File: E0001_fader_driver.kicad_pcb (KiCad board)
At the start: 4 copper layers, 107 x 17 mm, 34 parts, among them J1 JST GH SM04B-GHS-TB, J2 TC2030-IDC-NL, Q1 AO3401A, U1 STM32C051F6P6, U2 MCP1703A-3302E/CB, U3 DRV8210PDSGR

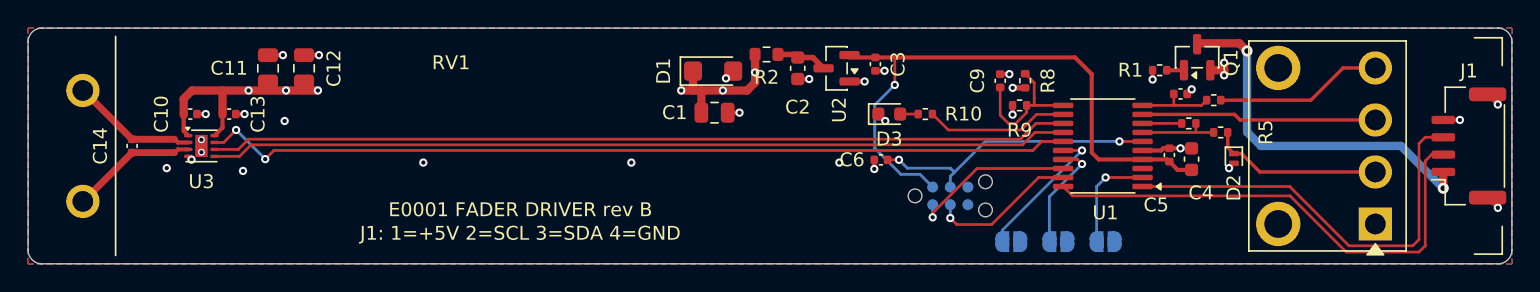
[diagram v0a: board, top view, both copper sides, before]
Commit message: E0001 rev C: PBUS v2 input, local eFuse, UART bootloader header, fab outputs
- Supply from E0003 peripheral bus v2 (PBUS 6-9 V) instead of 5 V
- TPS259470A local eFuse (OVLO, 0.6 A limit, reverse blocking); SMF9.0A after eFuse
- MCP1703A SOT-89 LDO; DRV8210 logic on 3V3
- Tag-Connect SWD replaced by 1x6 right-angle UART bootloader header (J2)
- No test points; common cross-project parts; PBUS 6-9 V silkscreen
- Rev B archived in archive/revB; fab outputs in fab/E0001_revB and fab/E0001_revC
- Spec docs/SPEC_revC.md v1.0, schematic notes, layout review r1 (PASS)

Co-Authored-By: Claude Opus 5.5 <noreply@anthropic.com>
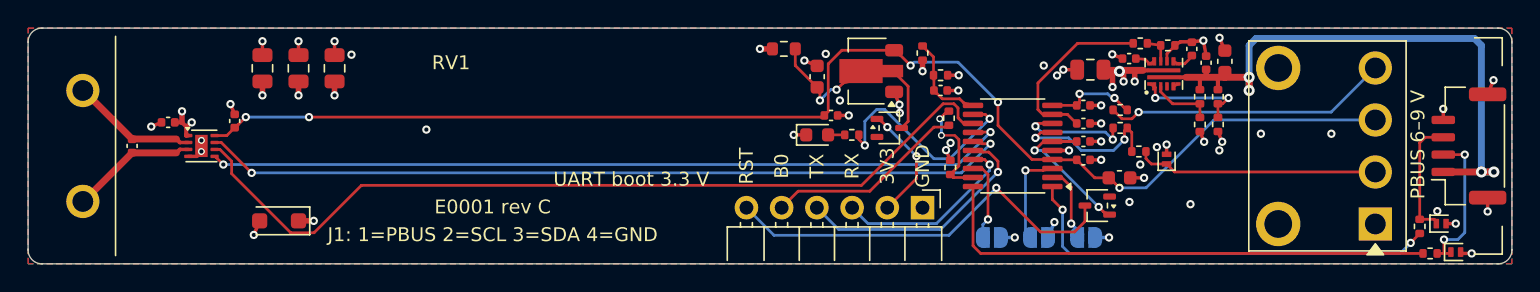
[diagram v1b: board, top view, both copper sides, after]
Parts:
- removed Q1: AO3401A, Package_TO_SOT_SMD:SOT-23
- removed R1: 10k, Resistor_SMD:R_0402_1005Metric
- added C15: 4.7nF, Capacitor_SMD:C_0402_1005Metric, F.Cu at (145.9, 93.7)
- added C16: 1.8nF, Capacitor_SMD:C_0402_1005Metric, F.Cu at (150.4, 93.0)
- added C17: 100nF, Capacitor_SMD:C_0402_1005Metric, F.Cu at (151.4, 94.0)
- added C18: 4.7uF, Capacitor_SMD:C_0603_1608Metric, F.Cu at (152.8, 93.9)
- added C19: 1nF, Capacitor_SMD:C_0402_1005Metric, F.Cu at (142.6, 98.4)
- added C20: 10uF, Capacitor_SMD:C_0805_2012Metric, F.Cu at (88.6, 94.4)
- added D4: PESD5V0L1UL, Diode_SMD:D_SOD-882, F.Cu at (169.4, 107.7)
- added D5: PESD5V0L1UL, Diode_SMD:D_SOD-882, F.Cu at (168.4, 105.6)
- added D6: BAT54W, Package_TO_SOT_SMD:SOT-323_SC-70, F.Cu at (143.6, 104.3)
- added D7: BAT54W, Package_TO_SOT_SMD:SOT-323_SC-70, F.Cu at (128.6, 98.7)
- added R11: 1M 1%, Resistor_SMD:R_0402_1005Metric, F.Cu at (152.3, 96.5)
- added R12: 330k 1%, Resistor_SMD:R_0402_1005Metric, F.Cu at (152.3, 98.5)
- added R13: 1M 1%, Resistor_SMD:R_0402_1005Metric, F.Cu at (151.0, 96.5)
- added R14: 137k 1%, Resistor_SMD:R_0402_1005Metric, F.Cu at (151.0, 98.5)
- added R15: 5.23k 1%, Resistor_SMD:R_0402_1005Metric, F.Cu at (148.7, 92.8)
- added R16: 10k, Resistor_SMD:R_0402_1005Metric, F.Cu at (146.7, 92.6)
- added R17: 10k, Resistor_SMD:R_0402_1005Metric, F.Cu at (133.0, 101.5)
- added R18: 1k, Resistor_SMD:R_0402_1005Metric, F.Cu at (132.9, 98.0)
- added R19: 0R, Resistor_SMD:R_0402_1005Metric, F.Cu at (167.6, 107.8)
- added R20: 0R, Resistor_SMD:R_0402_1005Metric, F.Cu at (166.8, 105.8)
- added U4: TPS259470ARPW, E0001:TI_RPW0010A_VQFN-HR-10_2x2mm_P0.475mm, F.Cu at (148.4, 94.8)
- C11, C12: value 22uF -> 10uF
- D1: value SMF5V0A -> SMF9.0A; footprint Diode_SMD:D_SMF -> Diode_SMD:D_SOD-123F
- J1: value JST GH SM04B-GHS-TB -> SM04B-GHS-TB
- J2: value TC2030-IDC-NL -> 61300611021; footprint Connector:Tag-Connect_TC2030-IDC-NL_2x03_P1.27mm_Vertical -> Connector_PinHeader_2.54mm:PinHeader_1x06_P2.54mm_Horizontal; moved to F.Cu
- R9: value 100k -> 30.1k 1%
- U2: value MCP1703A-3302E/CB -> MCP1703AT-3302E/MB; footprint Package_TO_SOT_SMD:SOT-23 -> Package_TO_SOT_SMD:SOT-89-3
- moved D1 33.1 mm to (84.6, 105.4), turned to 180 degrees
- moved C1 27.3 mm to (143.1, 94.5), turned to 180 degrees
- moved C6 14.7 mm to (142.6, 99.7), turned to 0 degrees
- moved R8 7.67 mm to (131.0, 93.3)
- moved C7 7.05 mm to (142.6, 97.1)
- moved R7 6.79 mm to (145.2, 97.4), turned to 0 degrees
- moved U1 6.50 mm to (137.5, 100.0)
- moved C4 6.21 mm to (142.6, 101.0), turned to 0 degrees
- moved R9 6.10 mm to (132.3, 94.9), turned to 0 degrees
- moved R5 6.06 mm to (146.6, 100.4)
- moved R10 5.51 mm to (125.9, 99.2)
- moved D3 5.41 mm to (123.4, 99.2)
- moved C5 5.37 mm to (145.2, 102.3), turned to 0 degrees
- moved R6 4.96 mm to (145.2, 98.7)
- moved C3 4.89 mm to (124.4, 97.8), turned to 0 degrees
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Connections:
- C1 pad 1: +5V -> VM_P
- C10 pad 1: +5V -> +3V3
- C11 pad 1: +5V -> VM_P
- C12 pad 1: +5V -> VM_P
- C13 pad 1: +5V -> VM_P
- D1 pad 1: +5V -> VM_P
- J1 pad 1: /VIN -> /PBUS_IN
- J1 pad 2: /I2C_SCL -> /J1_SCL
- J1 pad 3: /I2C_SDA -> /J1_SDA
- J2 pad 1: +3V3 -> GND
- J2 pad 2: /SWDIO -> /J2_3V3
- J2 pad 3: /NRST -> /UART_RX
- J2 pad 4: /SWCLK -> /UART_TX
- J2 pad 5: GND -> /J2_BOOT0
- J2 pad 6: unconnected-(J2-SWO-Pad6) -> /J2_NRST
- R2 pad 1: +5V -> VM_P
- R8 pad 1: +5V -> VM_P
- RV1 pad 3: /POT_HI -> +3V3
- U1 pad 16: /ADDR0 -> /UART_TX
- U1 pad 17: /ADDR1 -> /UART_RX
- U1 pad 18: /SWDIO -> /ADDR0
- U1 pad 19: /SWCLK -> /BOOT0
- U1 pad 3: unconnected-(U1-PC15-Pad3) -> /ADDR1
- U1 pad 9: /POT_HI -> /ILM_ADC
- U2 pad 2: +3V3 -> /LDO_IN
- U2 pad 3: /LDO_IN -> +3V3
- U3 pad 1: +5V -> VM_P
- U3 pad 8: +5V -> +3V3
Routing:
- net +3V3: track 43.8 -> 95.5 mm, vias 1 -> 5
- net /PBUS_IN: track 0.00 -> 42.7 mm, vias 0 -> 4
- net +5V: track 29.6 -> 0.00 mm, vias 9 -> 0
- net /J2_NRST: track 0.00 -> 29.4 mm, vias 0 -> 1
- net /VIN: track 26.7 -> 0.00 mm, vias 2 -> 0
- net /UART_TX: track 0.00 -> 18.3 mm, vias 0 -> 1
- net /POT_HI: track 17.0 -> 0.00 mm
- net GND: track 19.1 -> 34.9 mm, vias 29 -> 52
- net VM_P: track 0.00 -> 14.8 mm, vias 0 -> 12
- net /J2_BOOT0: track 0.00 -> 14.5 mm
- net /UART_RX: track 0.00 -> 13.8 mm, vias 0 -> 1
- net /ILM_ADC: track 0.00 -> 12.5 mm
- net /SWDIO: track 12.0 -> 0.00 mm, vias 1 -> 0
- net /LDO_IN: track 3.70 -> 15.1 mm, vias 0 -> 2
- net /J1_SCL: track 0.00 -> 10.9 mm, vias 0 -> 2
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- added copper zone on In2.Cu, net VM_P
- removed copper zone on In2.Cu, net +5V
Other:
- board text added: "3V3"
- board text added: "A0"
- board text added: "A1"
- board text added: "A2"
- board text added: "B0"
- board text added: "E0001 rev C"
- board text added: "GND"
- board text added: "J1: 1=PBUS 2=SCL 3=SDA 4=GND"
- board text added: "PBUS 6–9 V"
- board text added: "RST"
- board text added: "RX"
- board text added: "TX"
- board text added: "UART boot 3.3 V"
- board text added: "addr 0x30–0x37, open = 1"
- board text removed: "ADDR: bridge=0"
- board text removed: "E0001 FADER DRIVER rev B"
- board text removed: "J1: 1=+5V 2=SCL 3=SDA 4=GND"
- board text removed: "SWD (TC2030)"

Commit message: Rev C hand-route experiment: strip, scripted pre-route, Freerouting, cleanup
All tracks and vias of the rev C board removed; placement, footprints,
zones and net classes unchanged. Own scripts (build/hr, preroute_c.py)
hand-route the motor loop, U3 supply, eFuse U4 PBUS_IN/VM_P power,
the PBUS feed from J1, the touch nets, and a plane via for every
GND/VM_P SMD pad. Freerouting 2.5.0 routes the rest; cleanup.py rebuilds
the chains as 45-degree paths. Not TraceMaker. Some joins still to fix.

Co-Authored-By: Claude Opus 5.5 <noreply@anthropic.com>
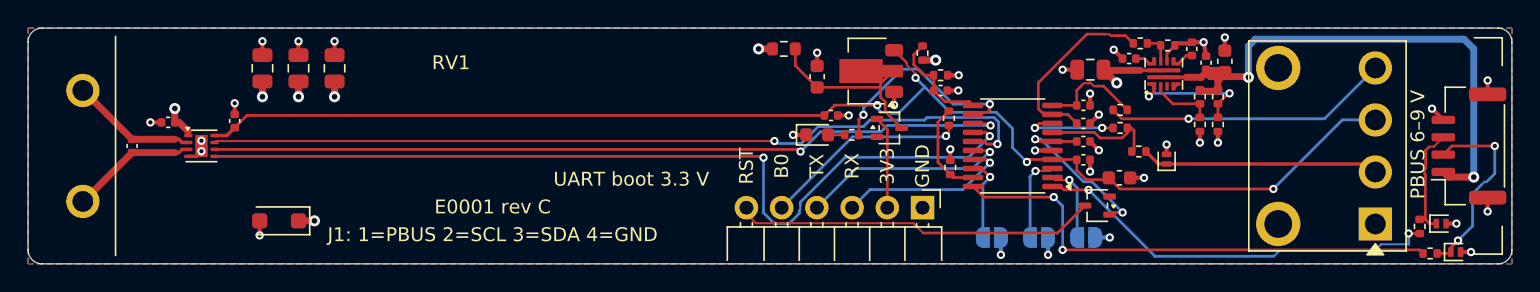
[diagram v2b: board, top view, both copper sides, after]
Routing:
- net /MOT_IN2: track 58.4 -> 64.6 mm
- net /MOT_IN1: track 62.6 -> 58.1 mm, vias 0 -> 2
- net /J2_NRST: track 29.4 -> 26.2 mm, vias 1 -> 0
- net /J1_SCL: track 10.9 -> 14.1 mm
- net /TOUCH_SNS: track 11.3 -> 8.14 mm, vias 2 -> 0
- net /UART_TX: track 18.3 -> 15.4 mm
- net /MOT_nSLEEP: track 59.0 -> 61.0 mm
- net /LDO_IN: track 15.1 -> 13.1 mm, vias 2 -> 0
- net GND: track 34.9 -> 36.7 mm, vias 52 -> 36
- net /J2_3V3: track 8.51 -> 6.71 mm, vias 2 -> 0
- net /PBUS_IN: track 42.7 -> 41.2 mm, vias 4 -> 2
- net /I2C_SDA: track 31.2 -> 29.8 mm
- net /ILM_ADC: track 12.5 -> 13.7 mm
- net /UART_RX: track 13.8 -> 12.6 mm
- net /TOUCH_DRV: track 8.13 -> 7.04 mm
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
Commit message: Rev C hand-route: DRC clean, no acute or right-angle joins
cleanup.py now recomputes chains after every rebuild (indices shifted).
fixes_c.py: PBUS_IN/VM_P at the eFuse and C13 enter each pad at separate
points, +3V3/LDO_IN/J1_SDA/I2C_SDA/FADER_POS/EF_OVLO joins redrawn at 45
degrees, LDO_IN ends on the U2 tab's anchor.

kicad-cli DRC with parity and refill: 0 errors, 0 unconnected, 0 parity;
the one warning (J2 lib_footprint_mismatch) is the same on master 43d01a5.
tm_viapad 0, slots 0, corners 0.

Co-Authored-By: Claude Opus 5.5 <noreply@anthropic.com>
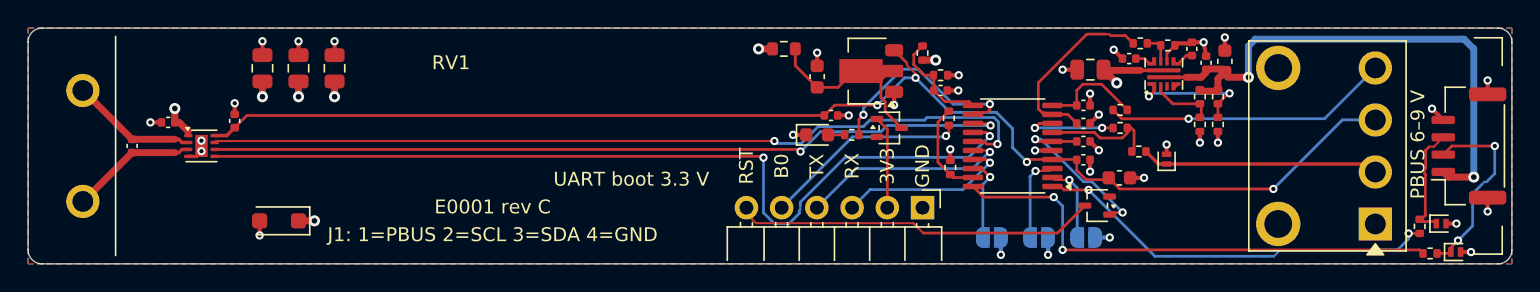
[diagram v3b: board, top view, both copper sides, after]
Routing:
- net /PBUS_IN: track 41.2 -> 37.6 mm
- net VM_P: track 14.7 -> 13.0 mm
- net +3V3: track 96.0 -> 94.8 mm
- net /LDO_IN: track 13.1 -> 13.8 mm
